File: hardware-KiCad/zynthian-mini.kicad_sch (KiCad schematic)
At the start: 37 parts, among them SW1 SW_Push, SW2 SW_Push, SW3 SW_Push, SW4 SW_Push, U1 74HCT14, U2 H11L1M

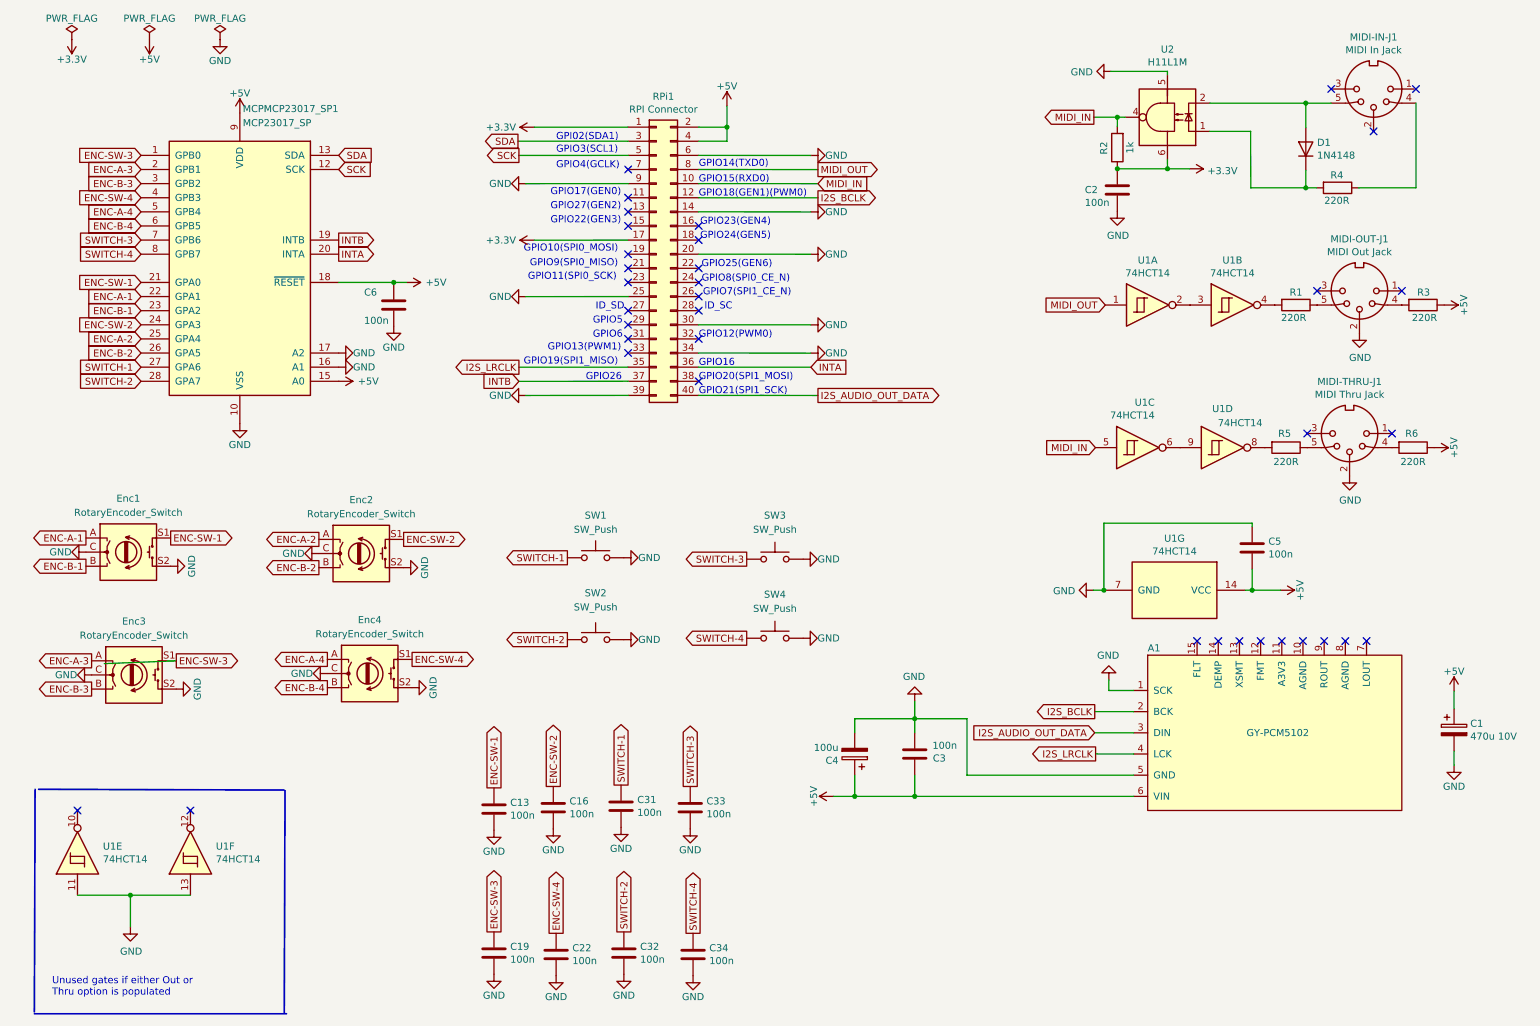
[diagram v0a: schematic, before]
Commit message: migration to KiCad 8.0
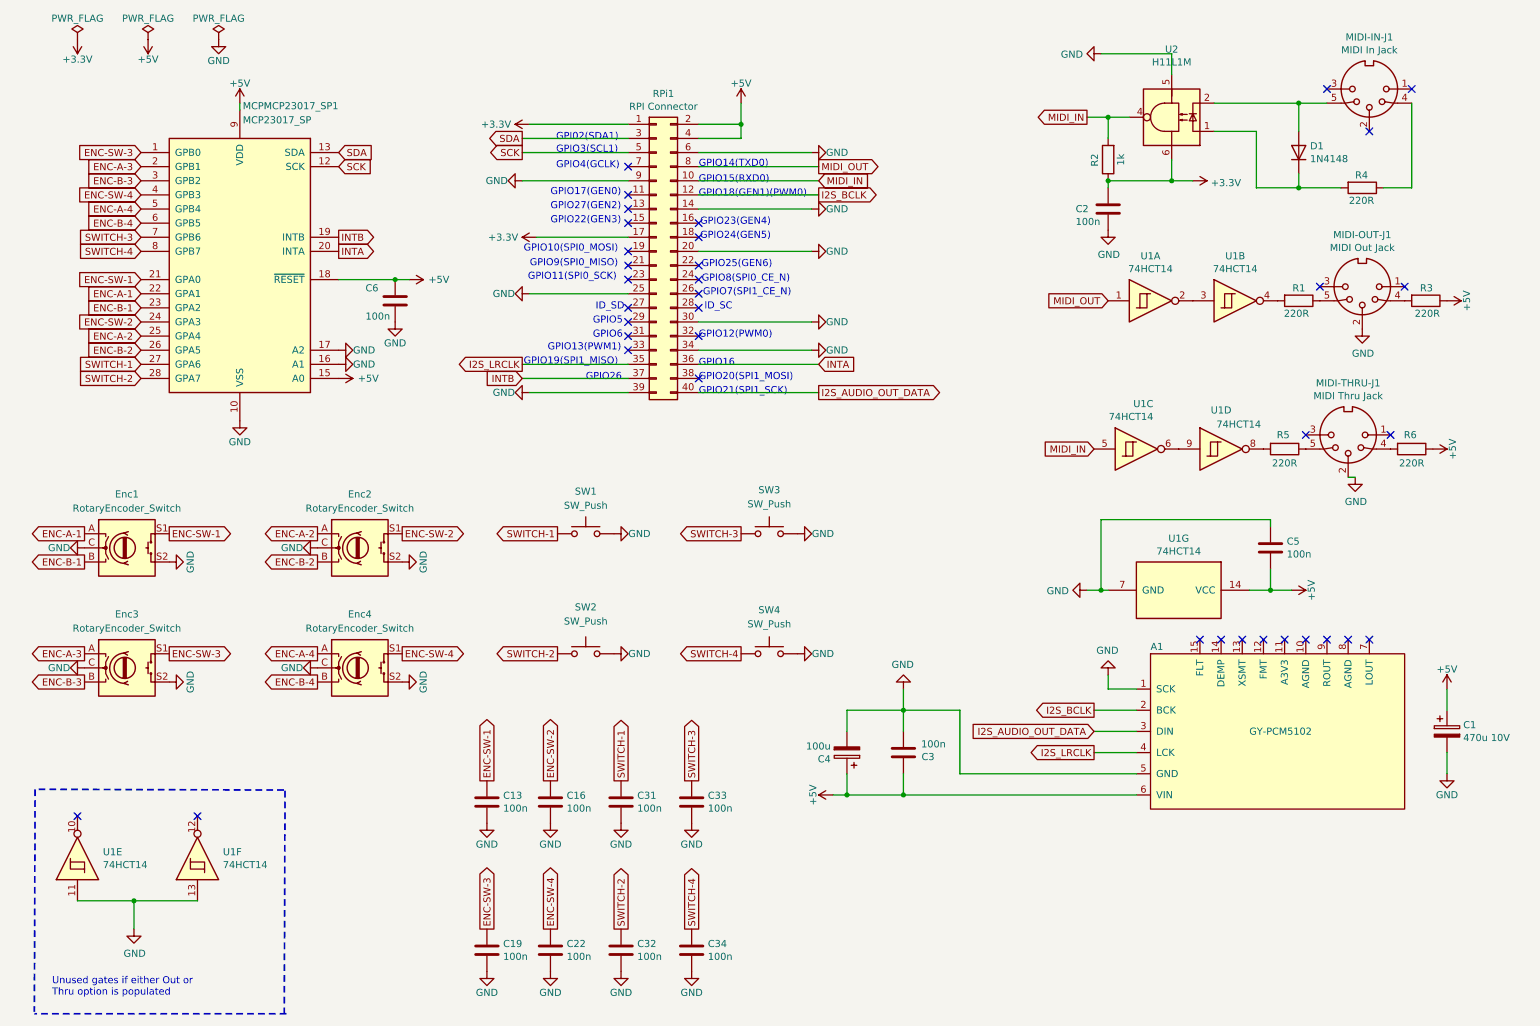
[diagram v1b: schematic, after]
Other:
- moved on the sheet: A1, C1, C13, C16, C19, C2, C22, C3, C31, C32, C33, C34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

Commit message: reverted back to v1-beta version for saving it into its own branch
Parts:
- A1: footprint project-footprints:GY-PCM5102 -> clumsyMIDI:GY-PCM5102
- MIDI-IN-J1, MIDI-OUT-J1, MIDI-THRU-J1: footprint project-footprints:MultiDIN5 -> My-Library:MultiDIN5
- SW1, SW2, SW3, SW4: footprint project-footprints:push-button -> My-Library:push-button
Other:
- moved on the sheet: A1, C1, C13, C16, C19, C2, C22, C3, C31, C32, C33, C34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
